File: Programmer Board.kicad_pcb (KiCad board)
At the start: 2 copper layers, 50 parts, among them J1 105-1103-001, J10 Conn_01x03, J11 105-1102-001, J12 105-1103-001, J13 Conn_01x02, J2 Conn_01x03, J3 105-1102-001, J4 UJ2-MIBH-4-SMT-TR, J5 5-5530843-4, J6 Conn_01x03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

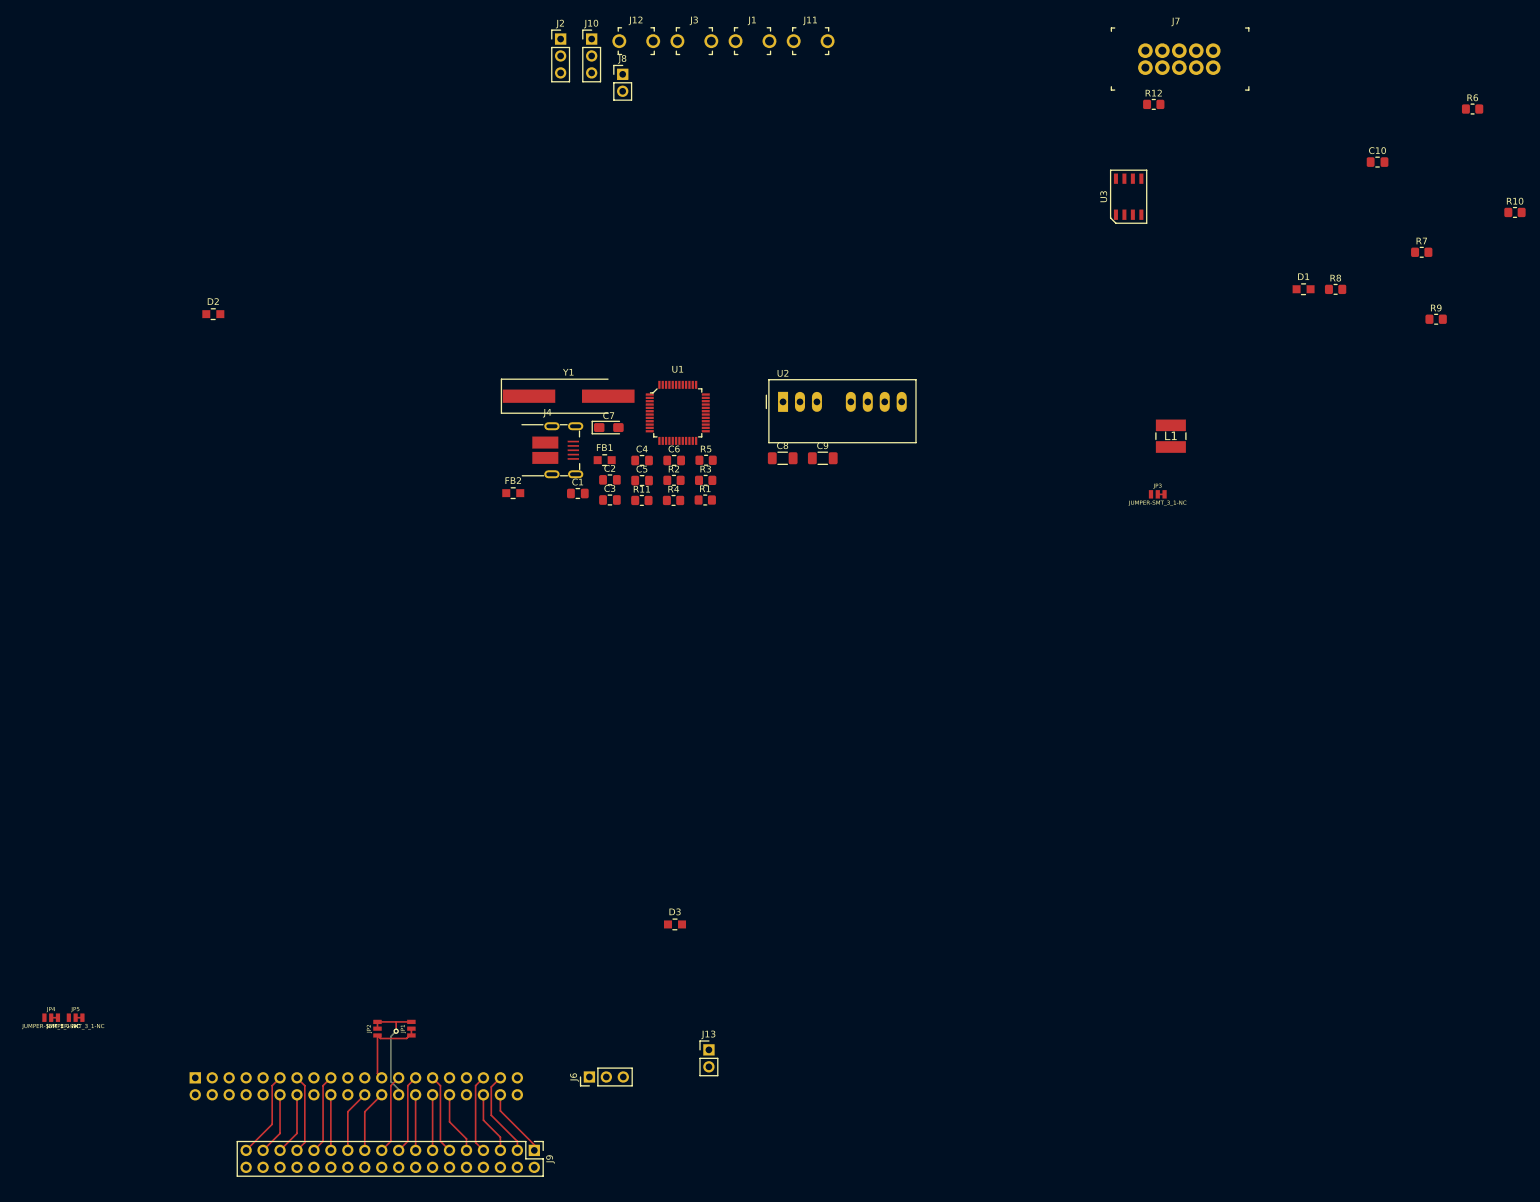
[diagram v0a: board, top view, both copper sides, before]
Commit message: Changed crystal for resonator. Board Layout.
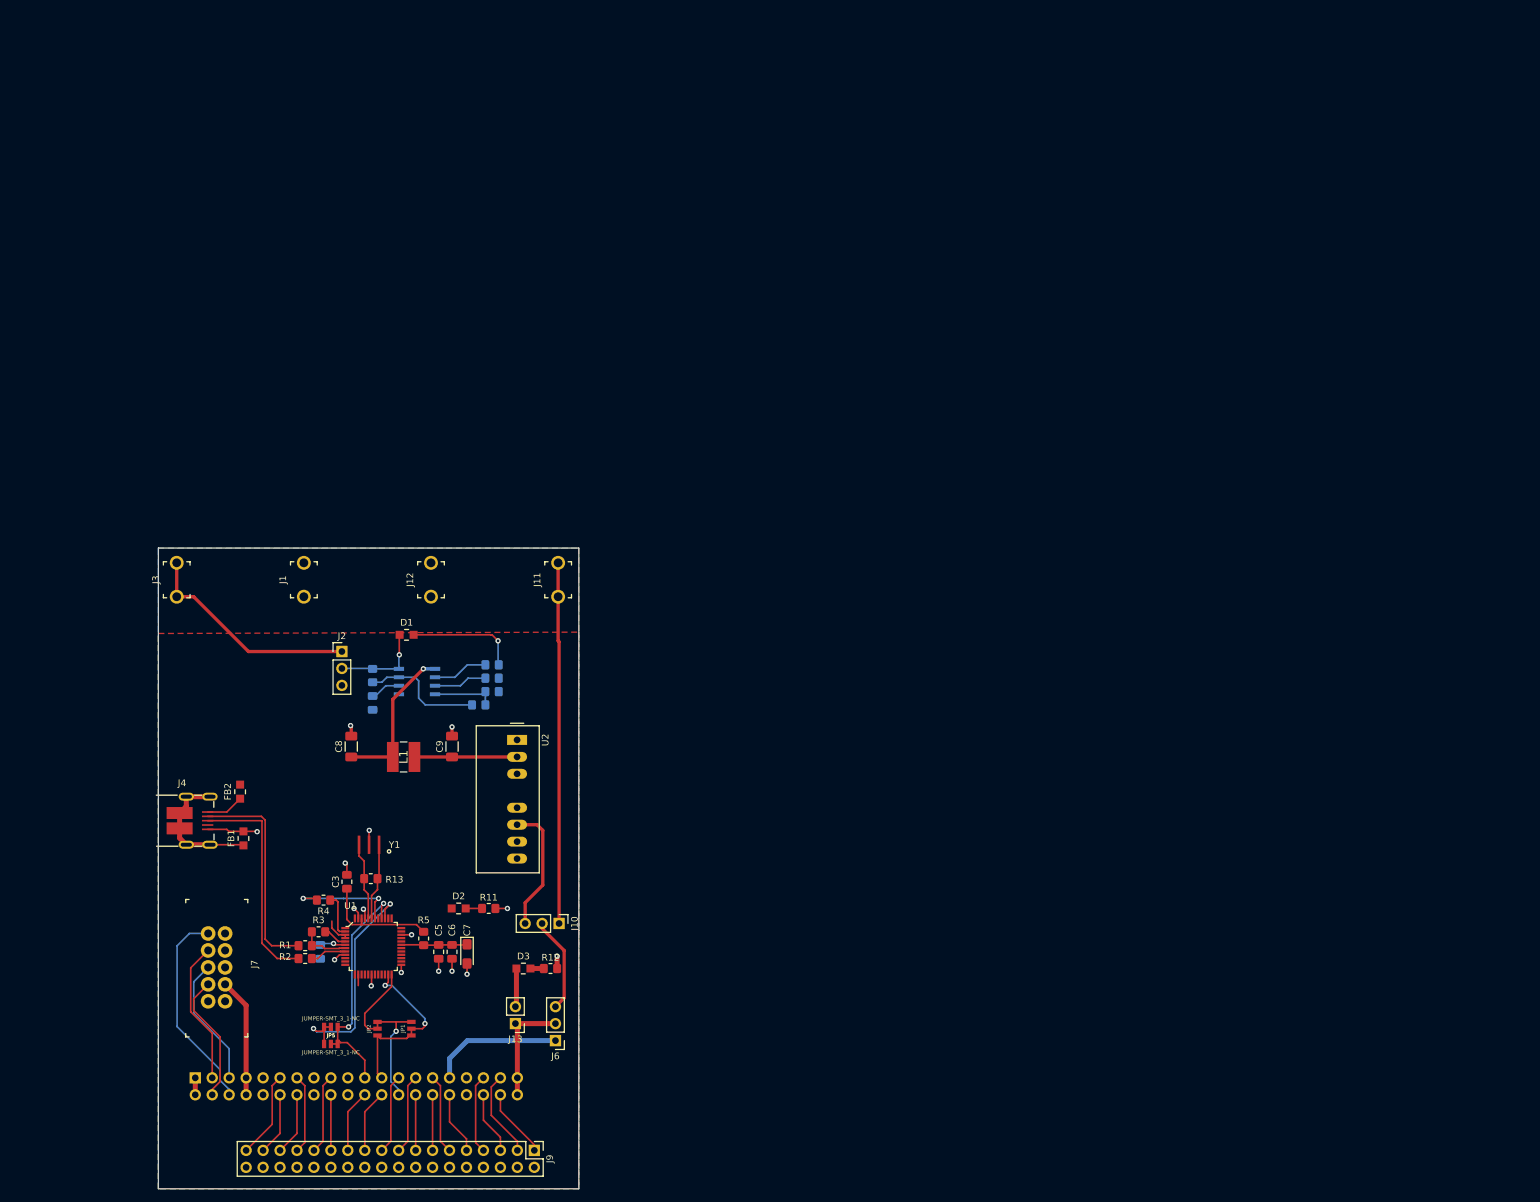
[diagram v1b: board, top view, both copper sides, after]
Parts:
- removed C1, C2: 12pF, Capacitor_SMD:C_0805_2012Metric_Pad1.18x1.45mm_HandSolder
- removed J8: Conn_01x02, Connector_PinHeader_2.54mm:PinHeader_1x02_P2.54mm_Vertical
- removed JP3: JUMPER-SMT_3_1-NC, Jumpers:SMT-JUMPER_3_1-NC_TRACE_NO-SILK
- added R13: 1M, Resistor_SMD:R_0805_2012Metric_Pad1.20x1.40mm_HandSolder, F.Cu at (139.3, 121.3)
- C10, C4, R10, R6, R7, R8, R9, U3: moved to B.Cu
- Y1: value AS-6.000-12-2020-EXT-SMD-TR -> CSTNR6M00GH5C000R0; footprint Crystal:Crystal_SMD_HC49-SD_HandSoldering -> LMS-6_Interface_Board:CSTNR_Resonator
- moved J7 191.1 mm to (117.5, 129.5), turned to 270 degrees
- moved R6 185.4 mm to (139.6, 90.8), turned to 270 degrees
- moved C10 171.0 mm to (139.6, 95.0), turned to 270 degrees
- moved R10 168.4 mm to (157.5, 91.2)
- moved R12 157.9 mm to (166.2, 134.8)
- moved R7 156.7 mm to (155.5, 95.2)
- moved R9 150.6 mm to (157.5, 89.2)
- moved D1 144.0 mm to (144.7, 84.8)
- moved R8 140.0 mm to (157.5, 93.3)
- moved J10 132.6 mm to (167.5, 128.0), turned to 270 degrees
- moved U3 129.0 mm to (146.2, 91.8), turned to 90 degrees
- moved L1 124.6 mm to (144.2, 103.0), turned to 270 degrees
- moved J3 111.9 mm to (110.2, 76.5), turned to 90 degrees
- moved J1 105.0 mm to (129.3, 76.5), turned to 90 degrees
- moved J2 97.5 mm to (135.0, 87.2)
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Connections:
- net Net-(C1-Pad1) renamed /USB to UART/XTIN
- net Net-(C4-Pad1) renamed /USB to UART/3V3OUT
- net Net-(J2-Pad1) renamed /+PS
- net Net-(J4-Pad2) renamed /USB to UART/USBDP_IN
- net Net-(J4-Pad3) renamed /USB to UART/USBDM_IN
- net Net-(R3-Pad1) renamed /USB to UART/RSTOUT
- J4 pad 4: Net-(J4-Pad4) -> (no net)
- J7 pad 9: Net-(J7-Pad9) -> (no net)
- JP4 pad 2: Net-(JP4-Pad2) -> /Card Edge Conn/U3.19
- JP4 pad 3: /USB to UART/UART2.TXD -> /Card Edge Conn/U3.19
- JP5 pad 1: /USB to UART/UART2.TXD -> /Card Edge Conn/U3.19
- JP5 pad 2: Net-(JP5-Pad2) -> /USB to UART/UART2.RXD
- R1 pad 1: Net-(R1-Pad1) -> /USB to UART/USBD_P
- R2 pad 1: Net-(R2-Pad1) -> /USB to UART/USBD_N
- R3 pad 2: Net-(R2-Pad1) -> /USB to UART/USBD_P
- U1 pad 1: Net-(U1-Pad1) -> (no net)
- U1 pad 10: Net-(U1-Pad10) -> (no net)
- U1 pad 11: Net-(U1-Pad11) -> (no net)
- U1 pad 12: Net-(U1-Pad12) -> (no net)
- U1 pad 13: Net-(U1-Pad13) -> (no net)
- U1 pad 15: Net-(U1-Pad15) -> (no net)
- U1 pad 16: Net-(U1-Pad16) -> (no net)
- U1 pad 17: Net-(U1-Pad17) -> (no net)
- U1 pad 19: Net-(U1-Pad19) -> (no net)
- U1 pad 20: Net-(U1-Pad20) -> (no net)
- U1 pad 21: Net-(U1-Pad21) -> (no net)
- U1 pad 22: Net-(U1-Pad22) -> (no net)
- U1 pad 26: Net-(U1-Pad26) -> (no net)
- U1 pad 27: Net-(U1-Pad27) -> (no net)
- U1 pad 28: Net-(U1-Pad28) -> (no net)
- U1 pad 29: Net-(U1-Pad29) -> (no net)
- U1 pad 30: Net-(U1-Pad30) -> (no net)
- U1 pad 32: Net-(U1-Pad32) -> (no net)
- U1 pad 33: Net-(U1-Pad33) -> (no net)
- U1 pad 35: Net-(U1-Pad35) -> (no net)
- U1 pad 36: Net-(U1-Pad36) -> (no net)
- U1 pad 37: Net-(U1-Pad37) -> (no net)
- U1 pad 38: Net-(U1-Pad38) -> (no net)
- U1 pad 39: Net-(JP5-Pad2) -> /USB to UART/UART2.RXD
- U1 pad 40: Net-(JP4-Pad2) -> /Card Edge Conn/U3.19
- U1 pad 41: Net-(U1-Pad41) -> (no net)
- U1 pad 44: Net-(C2-Pad1) -> /USB to UART/XOUT
- U1 pad 48: Net-(U1-Pad48) -> (no net)
- U1 pad 7: Net-(R1-Pad1) -> /USB to UART/USBD_P
- U1 pad 8: Net-(R2-Pad1) -> /USB to UART/USBD_N
- U2 pad 3: /DC-DC Converter/ON-~OFF -> (no net)
- U2 pad 5: Net-(U2-Pad5) -> (no net)
- U2 pad 8: Net-(U2-Pad8) -> (no net)
- Y1 pad 2: Net-(C2-Pad1) -> GND
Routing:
- net Net-(J10-Pad1): track 0.00 -> 54.1 mm
- net /Card Edge Conn/U3.19: track 0.00 -> 34.7 mm, vias 0 -> 2
- net /USB to UART/UART2.RXD: track 0.00 -> 33.7 mm, vias 0 -> 2
- net /+PS: track 0.00 -> 33.2 mm
- net GND: track 0.00 -> 33.1 mm, vias 0 -> 16
- net /USB to UART/USBDM_IN: track 0.00 -> 32.9 mm
- net /USB to UART/+5_USB: track 0.00 -> 32.2 mm, vias 0 -> 2
- net /USB to UART/USBDP_IN: track 0.00 -> 32.1 mm
- net /Card Edge Conn/ST7-ICCDATA: track 0.00 -> 31.0 mm
- net /DC-DC Converter/+V_in: track 0.00 -> 23.1 mm, vias 0 -> 1
- net /Card Edge Conn/ST7-ICCCLK: track 0.00 -> 21.5 mm
- net VDD: track 0.00 -> 20.4 mm
- net Net-(FB1-Pad1): track 0.00 -> 20.2 mm
- net +BATT: track 0.00 -> 19.9 mm
- net /Card Edge Conn/ST7-RESET: track 0.00 -> 19.6 mm
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- added copper zone on F.Cu, net /USB to UART/+5_USB
- added copper zone on B.Cu, net GND
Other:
- board outline added: 63 x 96 mm

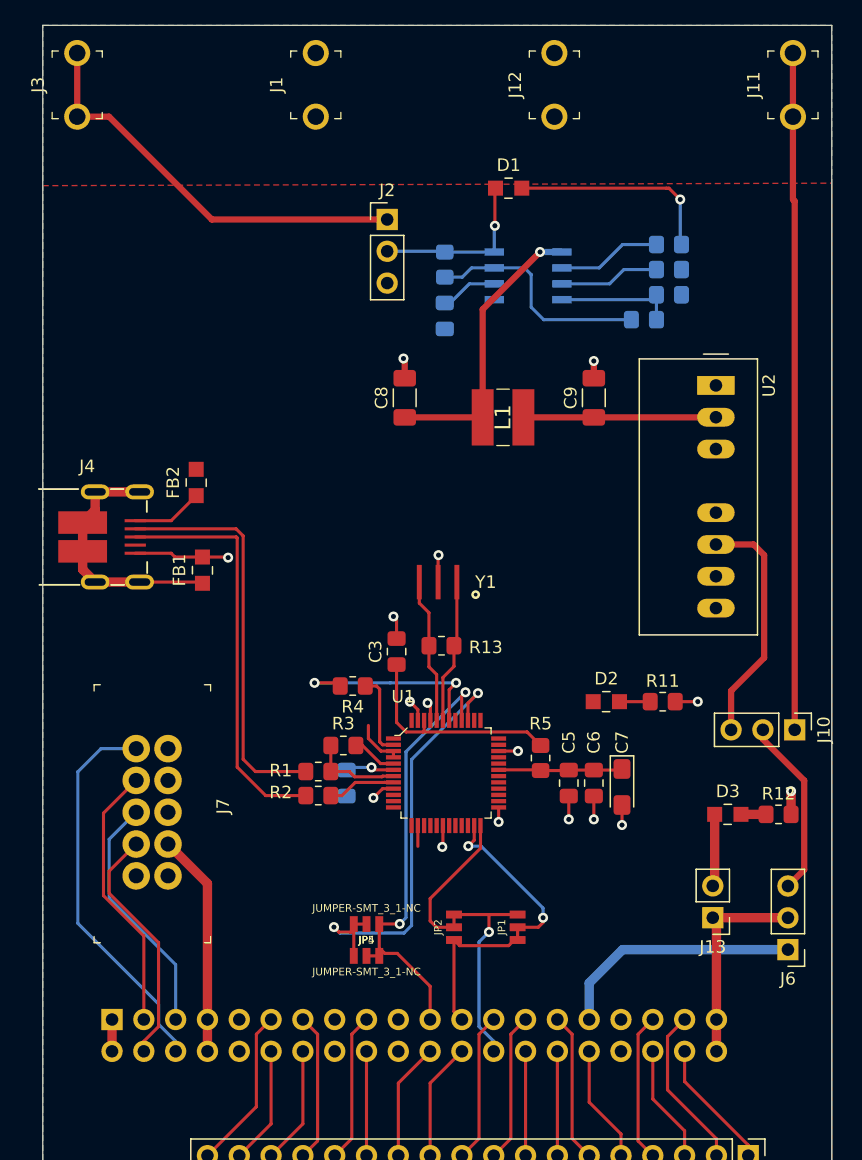
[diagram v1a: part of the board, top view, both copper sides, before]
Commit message: Fixed DRC Errors
Fixed drc errors
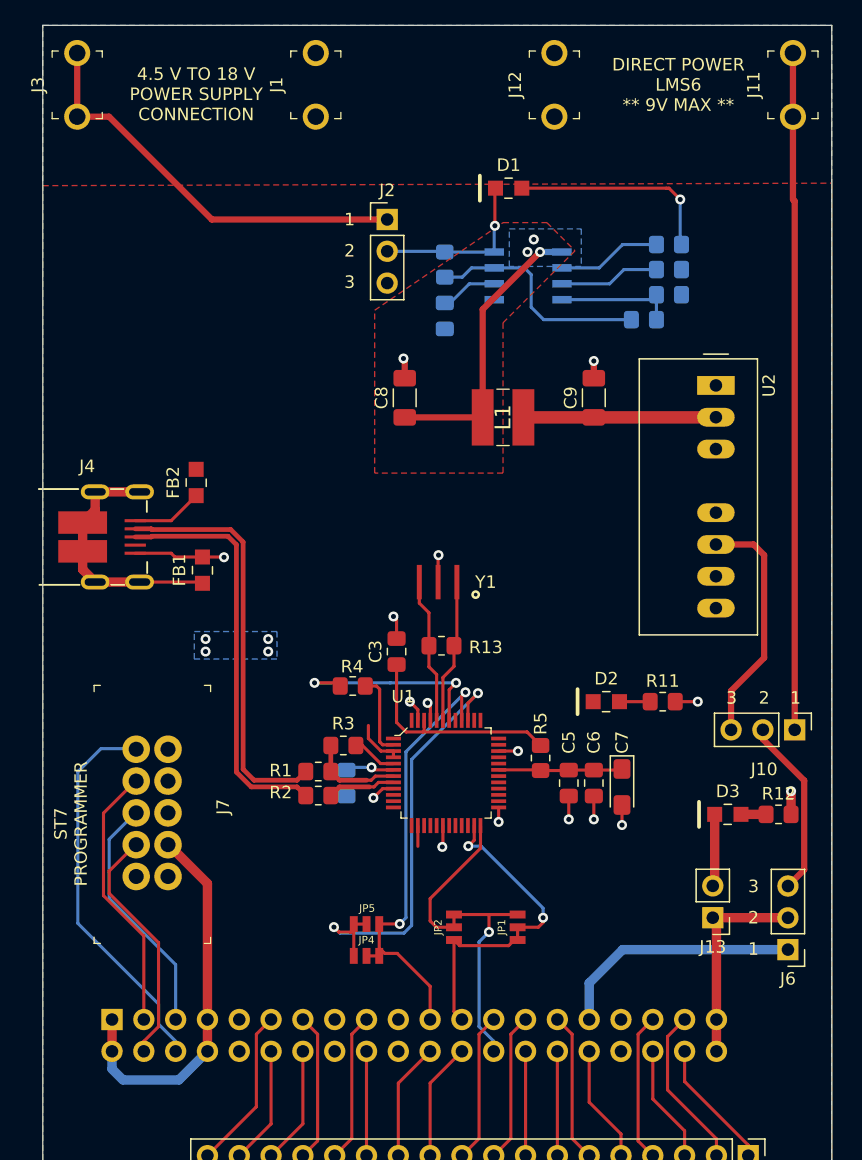
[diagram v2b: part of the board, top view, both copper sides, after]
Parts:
- U1: footprint digikey-footprints:LQFP-48_7x7mm -> LMS-6_Interface_Board:LQFP-48_7x7mm_Narrow_Pad
- moved J7 0.05 mm to (117.5, 129.6)
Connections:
- net /USB to UART/USBDM_IN renamed /USB to UART/IN_USBD_N
- net /USB to UART/USBDP_IN renamed /USB to UART/IN_USBD_P
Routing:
- net VDD: track 20.4 -> 30.7 mm
- net /USB to UART/IN_USBD_P: track 32.1 -> 32.8 mm
- net /USB to UART/+5_USB: vias 2 -> 6
- net /DC-DC Converter/+V_in: vias 1 -> 3
- added copper zone on B.Cu, net /DC-DC Converter/+V_in
- added copper zone on F.Cu, net /DC-DC Converter/+V_in
- added copper zone on B.Cu, net /USB to UART/+5_USB
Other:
- net class Default: clearance 0.2 -> 0.1524
- net class USB added: clearance 0.1524, trace_width 0.25, via_dia 0.8, via_drill 0.4
- rule trace_clearance: 0.2 -> 0.1524
- board text added: "1"
- board text added: "2"
- board text added: "3"
- board text added: "4.5 V TO 18 V POWER SUPPLY CONNECTION"
- board text added: "DIRECT POWER LMS6 ** 9V MAX **"
- board text added: "ST7 PROGRAMMER"

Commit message: Fabrication outputs
Added fabrication outputs
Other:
- board text added: "LMS6 INTERFACE REV. A GPL 3.0"

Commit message: Added SecKC Logo
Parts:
- added G***: LOGO, LMS-6_Interface_Board:faceoff_med, B.Cu at (139.0, 119.5)
